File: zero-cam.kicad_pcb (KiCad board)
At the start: 2 copper layers, 40 x 93 mm, 70 parts, among them J2 DC 12-24V, J4 Conn_01x04, Q1 tbd, Q2 tbd, U1 LMR36510, U2 Raspberry_Pi_ZeroW, U3 LP2985-3.3, U4 M24C02-FDW, U5 BME280, U6 ARJM11D7-114, U7 ENC424J600-PT, Y1 25MHz 50ppm

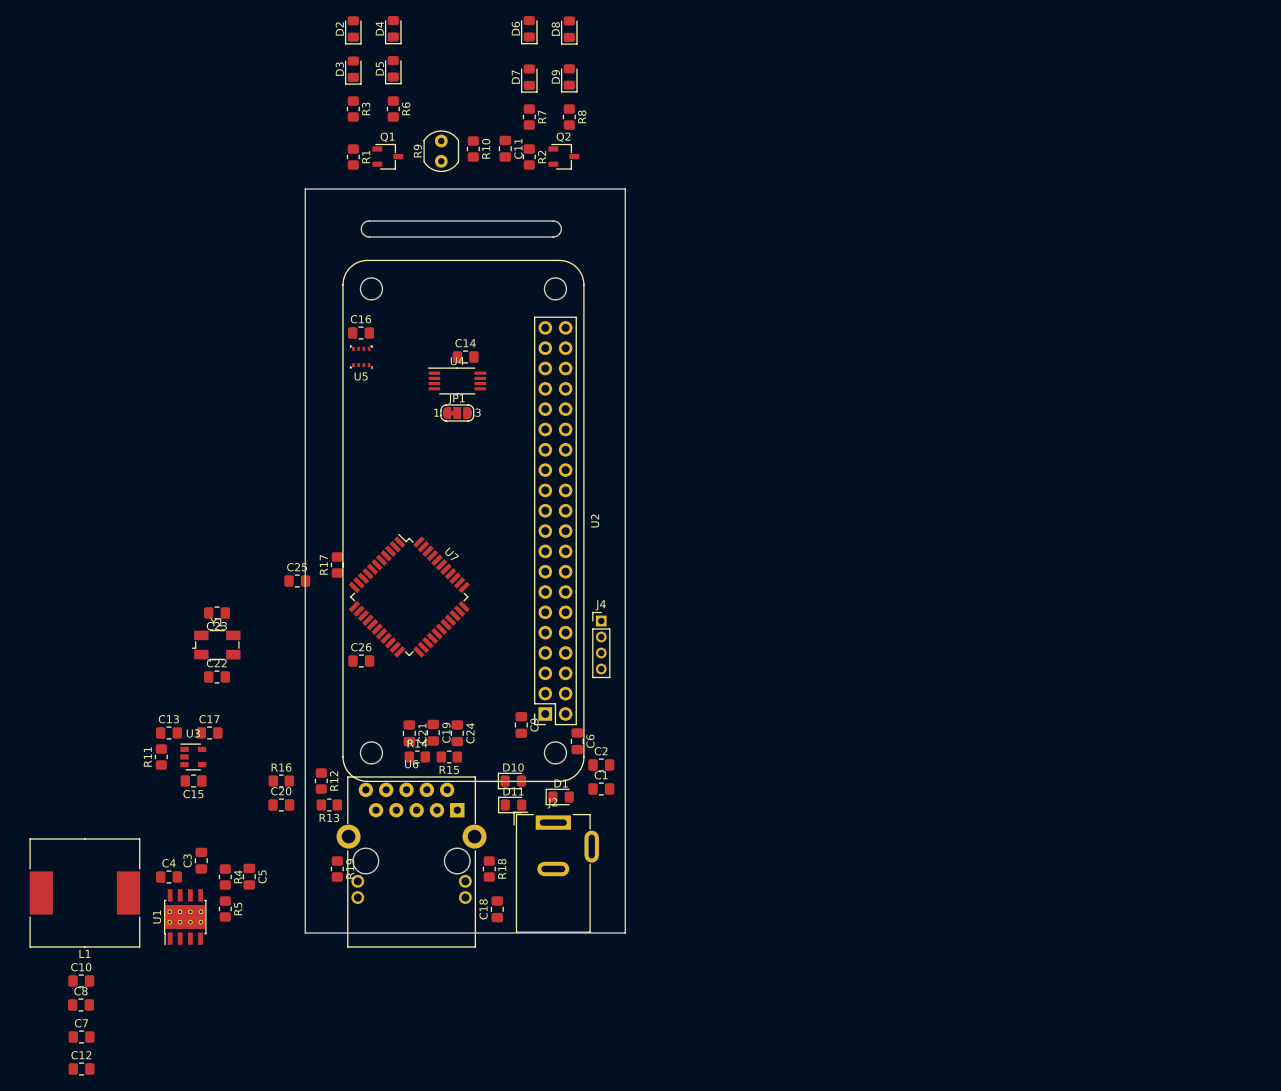
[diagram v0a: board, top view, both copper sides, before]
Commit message: Change for actual footprints, raff  board done.
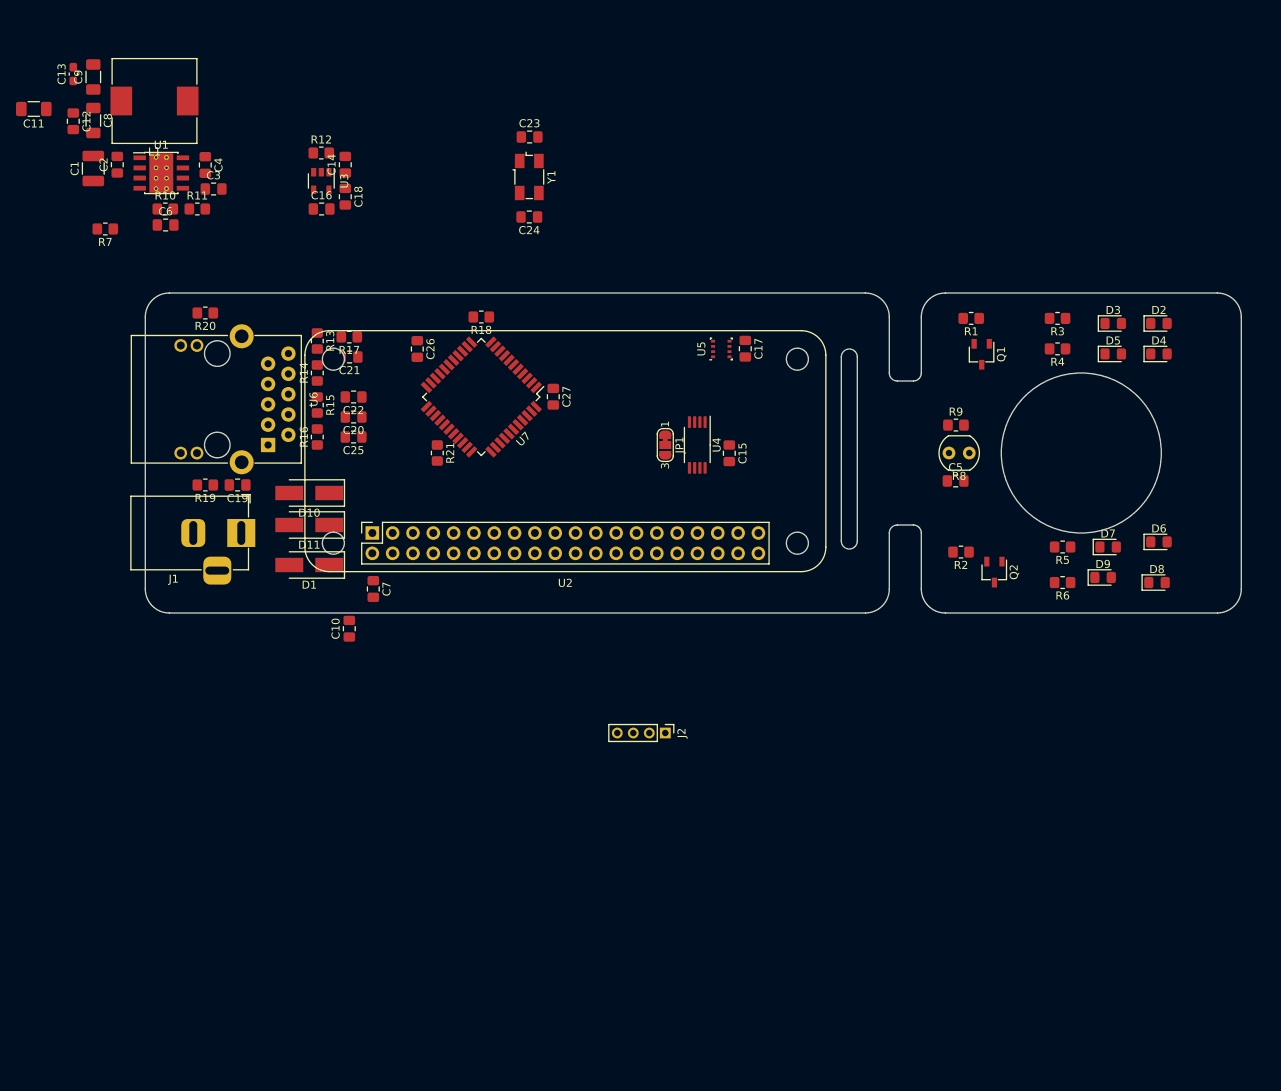
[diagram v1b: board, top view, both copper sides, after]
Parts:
- removed J4: Conn_01x04, Connector_PinHeader_2.00mm:PinHeader_1x04_P2.00mm_Vertical
- added C27: 0.1uF, Capacitor_SMD:C_0805_2012Metric_Pad1.18x1.45mm_HandSolder, F.Cu at (131.0, 83.0)
- added J1: DC 12-24V, Connector_BarrelJack:BarrelJack_Horizontal, F.Cu at (92.0, 100.0)
- added R20: 180, Resistor_SMD:R_0805_2012Metric_Pad1.20x1.40mm_HandSolder, F.Cu at (87.5, 72.5)
- added R21: 100k, Resistor_SMD:R_0805_2012Metric_Pad1.20x1.40mm_HandSolder, F.Cu at (116.5, 90.0)
- C1: footprint Capacitor_SMD:C_0805_2012Metric_Pad1.18x1.45mm_HandSolder -> Capacitor_SMD:C_1210_3225Metric_Pad1.33x2.70mm_HandSolder
- C10: value 10uF -> 0.1uF
- C11, C9: value 0.1uF -> 10uF; footprint Capacitor_SMD:C_0805_2012Metric_Pad1.18x1.45mm_HandSolder -> Capacitor_SMD:C_1206_3216Metric_Pad1.33x1.80mm_HandSolder
- C13: footprint Capacitor_SMD:C_0805_2012Metric_Pad1.18x1.45mm_HandSolder -> Capacitor_SMD:C_0603_1608Metric_Pad1.08x0.95mm_HandSolder
- C15: value 10nF -> 0.1uF
- C16: value 0.1uF -> 10nF
- C17: value 2.2uF -> 0.1uF
- C18: value 1000pF,2kV -> 2.2uF
- C19: value 0.1uF -> 1000pF,2kV
- C21: value 6.8nF,10% -> 0.1uF
- C22: value 15p -> 6.8nF,10%
- C24: value 6.8nF,10% -> 15p
- C25: value 10uF -> 6.8nF,10%
- C26: value 0.1uF -> 10uF
- C7: value 22uF -> 0.1uF
- C8: value 10uF -> 22uF; footprint Capacitor_SMD:C_0805_2012Metric_Pad1.18x1.45mm_HandSolder -> Capacitor_SMD:C_1206_3216Metric_Pad1.33x1.80mm_HandSolder
- D1: value tbd -> B160-13-F; footprint LED_SMD:LED_0805_2012Metric_Pad1.15x1.40mm_HandSolder -> Diode_SMD:D_SMA_Handsoldering
- D10, D11: value tbd -> B160-13-F; footprint Diode_SMD:D_0805_2012Metric_Pad1.15x1.40mm_HandSolder -> Diode_SMD:D_SMA_Handsoldering
- J2: value DC 12-24V -> Conn_01x04; footprint Connector_BarrelJack:BarrelJack_Wuerth_6941xx301002 -> Connector_PinHeader_2.00mm:PinHeader_1x04_P2.00mm_Vertical
- L1: footprint Inductor_SMD:L_Wuerth_HCM-1350 -> Inductor_SMD:L_10.4x10.4_H4.8
- R10: value 100R -> 100k
- R11: value 100k -> 24.9k
- R12: value 50R,1% -> 100k
- R16: value 10R, 1/12W,1% -> 50R,1%
- R17: value 12.4k,1% -> 10R, 1/12W,1%
- R18: value 180 -> 12.4k,1%
- R4: value 100k -> 100R
- R5: value 24.9k -> 100R
- R7: value 100R -> 10k
- R8: value 100R -> R_PHOTO; footprint Resistor_SMD:R_0805_2012Metric_Pad1.20x1.40mm_HandSolder -> OptoDevice:R_LDR_4.9x4.2mm_P2.54mm_Vertical
- R9: value R_PHOTO -> 100R; footprint OptoDevice:R_LDR_4.9x4.2mm_P2.54mm_Vertical -> Resistor_SMD:R_0805_2012Metric_Pad1.20x1.40mm_HandSolder
- moved R4 123.2 mm to (194.0, 77.0), turned to 180 degrees
- moved C12 118.5 mm to (71.0, 48.5), turned to 270 degrees
- moved R5 114.0 mm to (194.7, 101.8), turned to 180 degrees
- moved C8 110.6 mm to (73.5, 48.4), turned to 270 degrees
- moved D2 107.2 mm to (206.7, 73.8), turned to 0 degrees
- moved D4 104.0 mm to (206.7, 77.6), turned to 0 degrees
- moved R6 102.5 mm to (194.7, 106.2), turned to 180 degrees
- moved D6 101.5 mm to (206.7, 101.1), turned to 0 degrees
- moved C5 101.2 mm to (181.3, 93.5), turned to 0 degrees
- moved D8 100.9 mm to (206.5, 106.2), turned to 0 degrees
- moved C1 100.2 mm to (73.5, 54.4), turned to 90 degrees
- moved D3 100.2 mm to (201.0, 73.8), turned to 0 degrees
- moved L1 99.4 mm to (81.2, 46.0)
- moved C9 97.1 mm to (73.5, 43.0), turned to 90 degrees
- moved D5 96.8 mm to (201.0, 77.6), turned to 0 degrees
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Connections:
- C10 pad 1: +5V -> +3.3VA
- C11 pad 1: L_SENSE -> +5V
- C14 pad 1: GND -> +5V
- C14 pad 2: +3.3VA -> GND
- C15 pad 1: Net-(C15-Pad1) -> GND
- C15 pad 2: GND -> +3.3VA
- C16 pad 1: GND -> Net-(C16-Pad1)
- C16 pad 2: +3.3VA -> GND
- C17 pad 1: +3V3 -> GND
- C17 pad 2: GND -> +3.3VA
- C18 pad 1: Net-(C18-Pad1) -> +3V3
- C19 pad 1: GND -> Net-(C19-Pad1)
- C19 pad 2: Net-(C19-Pad2) -> GND
- C21 pad 1: Net-(C21-Pad1) -> GND
- C22 pad 2: GND -> Net-(C22-Pad2)
- C24 pad 2: Net-(C24-Pad2) -> GND
- C25 pad 2: GND -> Net-(C25-Pad2)
- C26 pad 1: GND -> Net-(C26-Pad1)
- C26 pad 2: +3V3 -> GND
- C5 pad 1: +5V -> L_SENSE
- C5 pad 2: Net-(C5-Pad2) -> GND
- C6 pad 1: GND -> +5V
- C6 pad 2: +5V -> Net-(C6-Pad2)
- C7 pad 1: +5V -> GND
- C7 pad 2: GND -> +5V
- C9 pad 1: +3.3VA -> +5V
- J2 pad 1: Net-(D1-Pad2) -> +3.3VA
- J2 pad 2: GND -> Net-(J2-Pad2)
- J2 pad 3: POE- -> Net-(J2-Pad3)
- R10 pad 1: L_SENSE -> +5V
- R10 pad 2: GND -> Net-(C6-Pad2)
- R11 pad 1: E_OFF -> Net-(C6-Pad2)
- R11 pad 2: +5V -> GND
- R12 pad 1: Net-(R12-Pad1) -> E_OFF
- R12 pad 2: Net-(C20-Pad2) -> +5V
- R13 pad 2: Net-(C20-Pad2) -> Net-(C21-Pad2)
- R14 pad 1: Net-(C21-Pad2) -> Net-(R14-Pad1)
- R14 pad 2: Net-(C19-Pad2) -> Net-(C21-Pad2)
- R15 pad 1: Net-(C24-Pad2) -> Net-(C22-Pad2)
- R15 pad 2: Net-(C19-Pad2) -> Net-(C20-Pad2)
- R16 pad 1: +3V3 -> Net-(C25-Pad2)
- R17 pad 1: Net-(R17-Pad1) -> +3V3
- R17 pad 2: GND -> Net-(C21-Pad2)
- R18 pad 2: Net-(R18-Pad2) -> GND
- R4 pad 1: +5V -> Net-(D5-Pad1)
- R4 pad 2: Net-(C5-Pad2) -> Net-(Q1-Pad1)
- R5 pad 1: Net-(C5-Pad2) -> Net-(D7-Pad1)
- R5 pad 2: GND -> Net-(Q2-Pad1)
- R6 pad 1: Net-(D5-Pad1) -> Net-(D9-Pad1)
- R6 pad 2: Net-(Q1-Pad1) -> Net-(Q2-Pad1)
- R7 pad 1: Net-(D7-Pad1) -> Net-(R7-Pad1)
- R7 pad 2: Net-(Q2-Pad1) -> PWR_GOOD
- R8 pad 1: Net-(D9-Pad1) -> +5V
- R8 pad 2: Net-(Q2-Pad1) -> L_SENSE
- R9 pad 1: +5V -> L_SENSE
- R9 pad 2: L_SENSE -> GND
- U1 pad 4: PWR_GOOD -> Net-(R7-Pad1)
- U1 pad 5: Net-(C5-Pad2) -> Net-(C6-Pad2)
- U2 pad 10: Net-(J4-Pad2) -> Net-(J2-Pad2)
- U2 pad 8: Net-(J4-Pad3) -> Net-(J2-Pad3)
- U3 pad 4: Net-(C15-Pad1) -> Net-(C16-Pad1)
- U6 pad 10: Net-(R12-Pad1) -> Net-(R13-Pad1)
- U6 pad 11: Net-(R18-Pad2) -> Net-(R19-Pad2)
- U6 pad 13: Net-(R19-Pad2) -> Net-(R20-Pad2)
- U6 pad 15: Net-(C18-Pad1) -> Net-(C19-Pad1)
- U6 pad 3: Net-(C24-Pad2) -> Net-(C25-Pad2)
- U6 pad 4: Net-(C19-Pad2) -> Net-(C20-Pad2)
- U6 pad 5: Net-(C21-Pad2) -> Net-(C22-Pad2)
- U6 pad 8: Net-(R13-Pad1) -> Net-(R14-Pad1)
- U6 pad 9: Net-(C20-Pad2) -> Net-(C21-Pad2)
- U7 pad 10: Net-(R18-Pad1) -> Net-(R19-Pad1)
- U7 pad 11: Net-(R17-Pad1) -> Net-(R18-Pad1)
- U7 pad 16: Net-(C21-Pad1) -> Net-(C22-Pad1)
- U7 pad 17: Net-(C24-Pad1) -> Net-(C25-Pad1)
- U7 pad 2: Net-(C23-Pad1) -> Net-(C24-Pad1)
- U7 pad 20: Net-(R12-Pad1) -> Net-(R13-Pad1)
- U7 pad 21: Net-(R13-Pad1) -> Net-(R14-Pad1)
- U7 pad 3: Net-(C22-Pad1) -> Net-(C23-Pad1)
- U7 pad 43: Net-(C25-Pad1) -> Net-(C26-Pad1)
- U7 pad 9: Net-(R19-Pad1) -> Net-(R20-Pad1)
- Y1 pad 1: Net-(C22-Pad1) -> Net-(C23-Pad1)
- Y1 pad 3: Net-(C23-Pad1) -> Net-(C24-Pad1)
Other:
- board size 40 x 93 mm -> 137 x 40 mm

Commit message: Connector placment done, dimentions decided ...
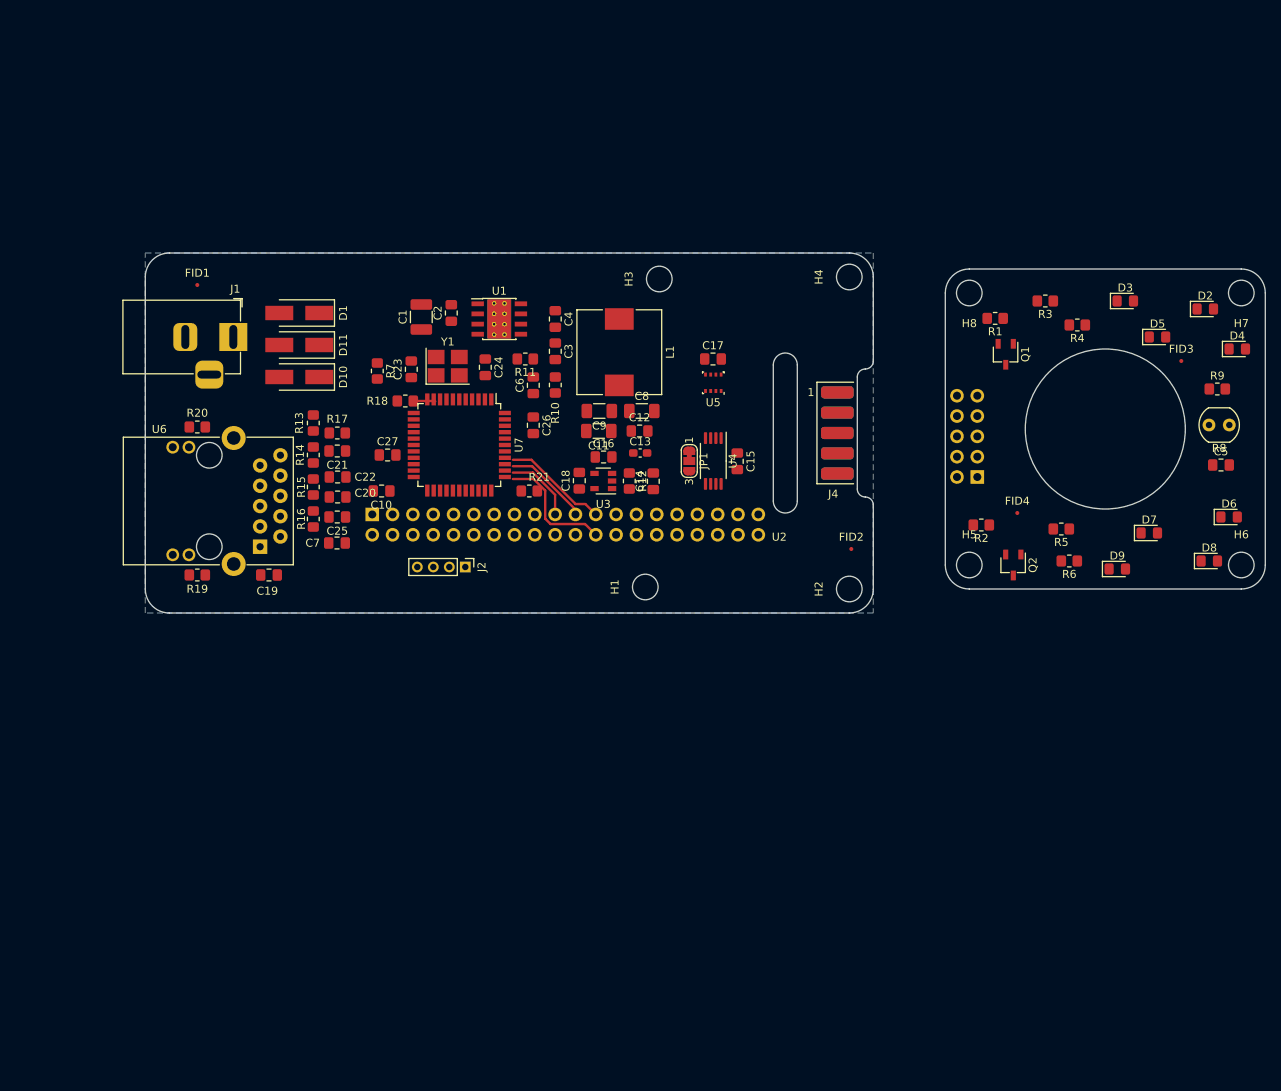
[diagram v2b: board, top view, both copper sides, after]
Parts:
- added FID1: Fiducial, Fiducial:Fiducial_0.5mm_Mask1mm, F.Cu at (86.5, 69.0)
- added FID2: Fiducial, Fiducial:Fiducial_0.5mm_Mask1mm, F.Cu at (168.2, 102.0)
- added FID3: Fiducial, Fiducial:Fiducial_0.5mm_Mask1mm, F.Cu at (209.5, 78.5)
- added FID4: Fiducial, Fiducial:Fiducial_0.5mm_Mask1mm, F.Cu at (189.0, 97.5)
- added H1: MountingHole, MountingHole:MountingHole_3.2mm_M3_DIN965, F.Cu at (142.5, 106.8)
- added H2: MountingHole, MountingHole:MountingHole_3.2mm_M3_DIN965, F.Cu at (168.0, 107.0)
- added H3: MountingHole, MountingHole:MountingHole_3.2mm_M3_DIN965, F.Cu at (144.2, 68.2)
- added H4: MountingHole, MountingHole:MountingHole_3.2mm_M3_DIN965, F.Cu at (168.0, 68.0)
- added H5: MountingHole, MountingHole:MountingHole_3.2mm_M3_DIN965, F.Cu at (183.0, 104.0)
- added H6: MountingHole, MountingHole:MountingHole_3.2mm_M3_DIN965, F.Cu at (217.0, 104.0)
- added H7: MountingHole, MountingHole:MountingHole_3.2mm_M3_DIN965, F.Cu at (217.0, 70.0)
- added H8: MountingHole, MountingHole:MountingHole_3.2mm_M3_DIN965, F.Cu at (183.0, 70.0)
- added J3: Conn_02x05_Top_Bottom, Connector_PinSocket_2.54mm:PinSocket_2x05_P2.54mm_Vertical, B.Cu at (184.0, 93.0)
- added J4: Conn_02x05_Top_Bottom, zero-cam:Edge_PinHeader_2x05_P2, F.Cu at (166.5, 87.5)
- Y1: footprint Crystal:Crystal_SMD_Abracon_ABM3B-4Pin_5.0x3.2mm -> Crystal:Crystal_SMD_3225-4Pin_3.2x2.5mm_HandSoldering
- moved C13 85.2 mm to (141.9, 90.0), turned to 0 degrees
- moved C11 81.3 mm to (136.7, 87.2)
- moved C12 80.7 mm to (141.8, 87.2), turned to 0 degrees
- moved C8 77.6 mm to (142.1, 84.8), turned to 0 degrees
- moved C9 75.8 mm to (136.8, 84.8), turned to 180 degrees
- moved L1 66.0 mm to (139.2, 77.4), turned to 270 degrees
- moved R12 56.2 mm to (140.5, 93.5), turned to 270 degrees
- moved C14 55.2 mm to (143.5, 93.5)
- moved R10 53.5 mm to (131.2, 81.5), turned to 90 degrees
- moved U3 51.5 mm to (137.2, 93.5), turned to 180 degrees
- moved C6 50.1 mm to (128.5, 81.5), turned to 90 degrees
- moved C4 47.8 mm to (131.2, 73.2)
- moved C3 47.3 mm to (131.2, 77.3), turned to 270 degrees
- moved C16 46.9 mm to (137.3, 90.5)
- moved U1 46.0 mm to (124.2, 73.2)
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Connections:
- net Net-(C20-Pad2) renamed /ethernet_if/rct
- net Net-(C21-Pad2) renamed /ethernet_if/TCT
- net Net-(C22-Pad1) renamed /ethernet_if/TP_IN+
- net Net-(C22-Pad2) renamed /ethernet_if/rd+
- net Net-(C25-Pad1) renamed /ethernet_if/TP_IN-
- net Net-(C25-Pad2) renamed /ethernet_if/rd-
- net Net-(C26-Pad1) renamed /ethernet_if/e_vcap
- net Net-(C4-Pad1) renamed /sw
- net Net-(C4-Pad2) renamed /boot
- net Net-(C6-Pad2) renamed /fb
- net Net-(JP1-Pad2) renamed /WC
- net Net-(R13-Pad1) renamed /ethernet_if/TP_OUT+
- net Net-(R14-Pad1) renamed /ethernet_if/TP_OUT-
- net Net-(R18-Pad1) renamed /ethernet_if/e_bias
- net Net-(R19-Pad1) renamed /ethernet_if/led_a
- net Net-(R20-Pad1) renamed /ethernet_if/led_b
- net Net-(R7-Pad1) renamed /pg
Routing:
- net /ethernet_if/~E_CS~: track 0.00 -> 15.3 mm
- net /ethernet_if/E_SCK: track 0.00 -> 13.2 mm
- net /ethernet_if/E_MOSI: track 0.00 -> 10.7 mm
- net /ethernet_if/E_MISO: track 0.00 -> 8.88 mm
- net /ethernet_if/e_bias: track 0.00 -> 2.77 mm
- added copper zone on B.Cu, net GND
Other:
- board size 137 x 40 mm -> 140 x 45 mm
- net class Default: trace_width 0.25 -> 0.3; via_dia 0.8 -> 0.45; via_drill 0.4 -> 0.35
- net class Power added: clearance 0.3, trace_width 0.3, via_dia 0.45, via_drill 0.35
- net class Signal added: clearance 0.2, trace_width 0.3, via_dia 0.45, via_drill 0.35
- net class ethernet_sig added: clearance 0.2, trace_width 0.3, via_dia 0.45, via_drill 0.35

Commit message: start layout
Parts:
- J3: value Conn_02x05_Top_Bottom -> Front_Plate
- J4: value Conn_02x05_Top_Bottom -> Edge_Connector
- moved C14 11.1 mm to (133.8, 88.2), turned to 180 degrees
- moved C18 10.1 mm to (143.8, 90.0), turned to 270 degrees
- moved C12 8.13 mm to (133.8, 86.0), turned to 180 degrees
- moved C13 8.12 mm to (133.8, 90.2), turned to 180 degrees
- moved R12 4.78 mm to (137.2, 90.0), turned to 90 degrees
- moved U3 4.78 mm to (140.5, 90.0), turned to 0 degrees
- moved C16 4.07 mm to (140.5, 93.0), turned to 180 degrees
- moved C9 3.25 mm to (133.8, 83.5)
- moved C8 3.08 mm to (139.2, 83.5)
- moved L1 2.98 mm to (136.5, 76.2)
- moved C11 2.75 mm to (139.2, 86.2), turned to 0 degrees
- moved R18 2.26 mm to (110.2, 83.2)
- moved R10 2.02 mm to (129.5, 80.5)
- moved C3 1.92 mm to (129.5, 76.5)
- moved C4 1.90 mm to (129.5, 72.5)
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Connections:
- J3 pad 1: (no net) -> +5V
- J3 pad 10: (no net) -> GND
- J3 pad 2: (no net) -> L_SENSE
- J3 pad 3: (no net) -> PWM_1
- J3 pad 4: (no net) -> PWM_0
- J3 pad 5: (no net) -> GND
- J3 pad 6: (no net) -> +5V
- J4 pad 1: (no net) -> +5V
- J4 pad 10: (no net) -> GND
- J4 pad 2: (no net) -> L_SENSE
- J4 pad 3: (no net) -> PWM_1
- J4 pad 4: (no net) -> PWM_0
- J4 pad 5: (no net) -> GND
- J4 pad 6: (no net) -> +5V
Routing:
- net +3V3: track 0.00 -> 33.2 mm
- net +5V: track 0.00 -> 29.5 mm, vias 0 -> 4
- net GND: track 0.00 -> 28.4 mm, vias 0 -> 13
- net /ethernet_if/TP_OUT+: track 0.00 -> 25.1 mm
- net /ethernet_if/TP_OUT-: track 0.00 -> 17.7 mm
- net E_INT: track 0.00 -> 16.1 mm
- net /ethernet_if/TP_IN-: track 0.00 -> 14.1 mm, vias 0 -> 2
- net /ethernet_if/TCT: track 0.00 -> 14.1 mm
- net /ethernet_if/rd+: track 0.00 -> 11.3 mm
- net /ethernet_if/TP_IN+: track 0.00 -> 10.5 mm, vias 0 -> 2
- net Net-(C23-Pad1): track 0.00 -> 10.2 mm
- net /sw: track 0.00 -> 9.85 mm
- net /ethernet_if/rd-: track 0.00 -> 9.77 mm
- net Net-(C24-Pad1): track 0.00 -> 9.55 mm
- net /ethernet_if/rct: track 0.00 -> 8.48 mm
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- added copper zone on F.Cu, net +5V
- added copper zone on F.Cu, net GND
- added copper zone on F.Cu, net POE+
